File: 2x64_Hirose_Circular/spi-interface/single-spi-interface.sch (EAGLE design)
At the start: 30 parts, among them Q1 SSM3K324, Q2 SSM3J328

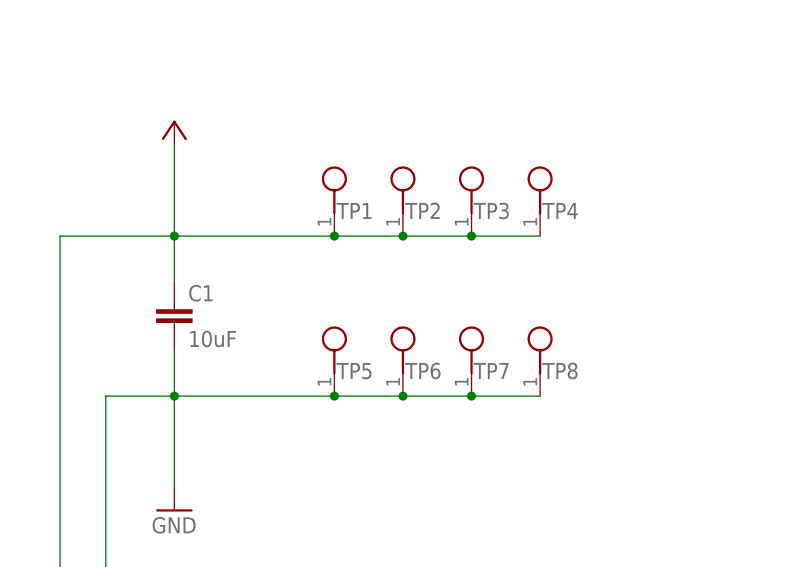
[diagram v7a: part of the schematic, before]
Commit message: Rev 1.1 of heastage, eib, and interface. All sent out for quotes.
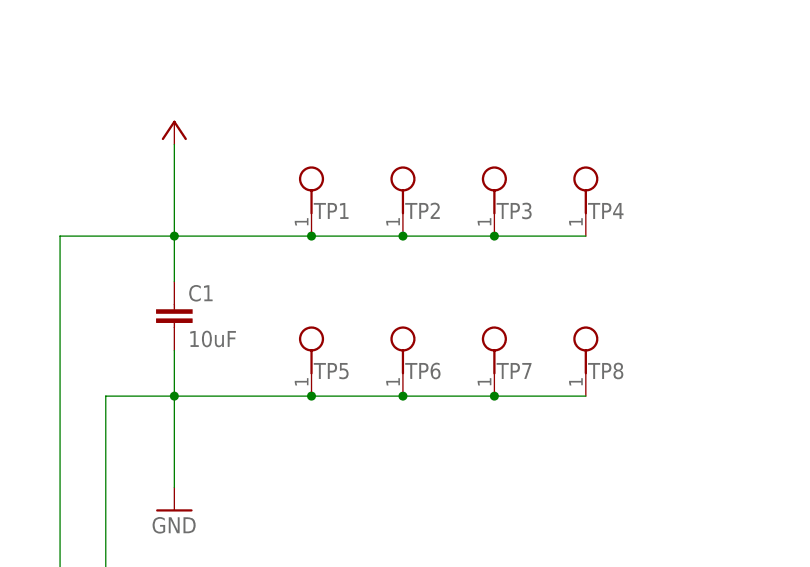
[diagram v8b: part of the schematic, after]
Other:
- moved on the sheet: TP1, TP3, TP4, TP5, TP7, TP8
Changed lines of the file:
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@@
 <instance part="ANT" gate="D$1" x="165.1" y="228.6"/>
 <instance part="POST" gate="D$1" x="233.68" y="228.6"/>
-<instance part="TP1" gate="TP$1" x="93.98" y="261.62"/>
+<instance part="TP1" gate="TP$1" x="91.44" y="261.62"/>
 <instance part="TP2" gate="TP$1" x="101.6" y="261.62"/>
-<instance part="TP3" gate="TP$1" x="109.22" y="261.62"/>
-<instance part="TP4" gate="TP$1" x="116.84" y="261.62"/>
-<instance part="TP5" gate="TP$1" x="93.98" y="243.84"/>
+<instance part="TP3" gate="TP$1" x="111.76" y="261.62"/>
+<instance part="TP4" gate="TP$1" x="121.92" y="261.62"/>
+<instance part="TP5" gate="TP$1" x="91.44" y="243.84"/>
 <instance part="TP6" gate="TP$1" x="101.6" y="243.84"/>
-<instance part="TP7" gate="TP$1" x="109.22" y="243.84"/>
-<instance part="TP8" gate="TP$1" x="116.84" y="243.84"/>
+<instance part="TP7" gate="TP$1" x="111.76" y="243.84"/>
+<instance part="TP8" gate="TP$1" x="121.92" y="243.84"/>
 </instances>
 <busses>
@@
 <label x="55.88" y="208.28" size="1.778" layer="95"/>
 <pinref part="TP5" gate="TP$1" pin="1"/>
-<wire x1="76.2" y1="236.22" x2="93.98" y2="236.22" width="0.1524" layer="91"/>
+<wire x1="76.2" y1="236.22" x2="91.44" y2="236.22" width="0.1524" layer="91"/>
 <pinref part="TP6" gate="TP$1" pin="1"/>
-<wire x1="93.98" y1="236.22" x2="101.6" y2="236.22" width="0.1524" layer="91"/>
-<junction x="93.98" y="236.22"/>
+<wire x1="91.44" y1="236.22" x2="101.6" y2="236.22" width="0.1524" layer="91"/>
+<junction x="91.44" y="236.22"/>
 <pinref part="TP7" gate="TP$1" pin="1"/>
-<wire x1="101.6" y1="236.22" x2="109.22" y2="236.22" width="0.1524" layer="91"/>
+<wire x1="101.6" y1="236.22" x2="111.76" y2="236.22" width="0.1524" layer="91"/>
 <junction x="101.6" y="236.22"/>
 <pinref part="TP8" gate="TP$1" pin="1"/>
-<wire x1="109.22" y1="236.22" x2="116.84" y2="236.22" width="0.1524" layer="91"/>
-<junction x="109.22" y="236.22"/>
+<wire x1="111.76" y1="236.22" x2="121.92" y2="236.22" width="0.1524" layer="91"/>
+<junction x="111.76" y="236.22"/>
 </segment>
 <segment>
@@
 <label x="55.88" y="210.82" size="1.778" layer="95"/>
 <pinref part="TP1" gate="TP$1" pin="1"/>
-<wire x1="76.2" y1="254" x2="93.98" y2="254" width="0.1524" layer="91"/>
+<wire x1="76.2" y1="254" x2="91.44" y2="254" width="0.1524" layer="91"/>
 <pinref part="TP2" gate="TP$1" pin="1"/>
-<wire x1="93.98" y1="254" x2="101.6" y2="254" width="0.1524" layer="91"/>
-<junction x="93.98" y="254"/>
+<wire x1="91.44" y1="254" x2="101.6" y2="254" width="0.1524" layer="91"/>
+<junction x="91.44" y="254"/>
 <pinref part="TP3" gate="TP$1" pin="1"/>
-<wire x1="101.6" y1="254" x2="109.22" y2="254" width="0.1524" layer="91"/>
+<wire x1="101.6" y1="254" x2="111.76" y2="254" width="0.1524" layer="91"/>
 <junction x="101.6" y="254"/>
 <pinref part="TP4" gate="TP$1" pin="1"/>
-<wire x1="109.22" y1="254" x2="116.84" y2="254" width="0.1524" layer="91"/>
-<junction x="109.22" y="254"/>
-</segment>
-<segment>
+<wire x1="111.76" y1="254" x2="121.92" y2="254" width="0.1524" layer="91"/>
+<junction x="111.76" y="254"/>
+</segment>
+<segment>
